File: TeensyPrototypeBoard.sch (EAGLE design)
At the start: 50 parts, among them Q1 16mhz, SW1 SPST_TACT-KMR2, SW2 SPST_TACT-KMR2, U3 BLE112-A, U4 MPU-6050-1, X1 32.768khz

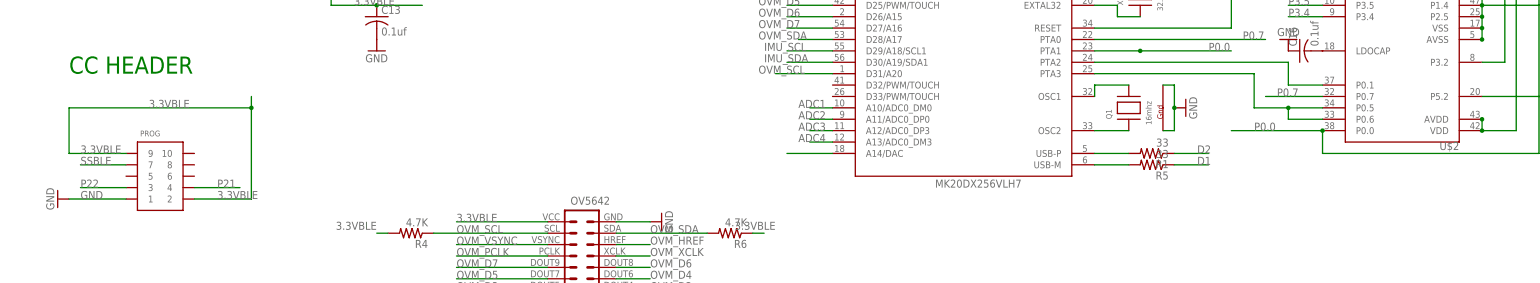
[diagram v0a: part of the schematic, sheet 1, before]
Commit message: connect the oscillator and add generate BOM.txt
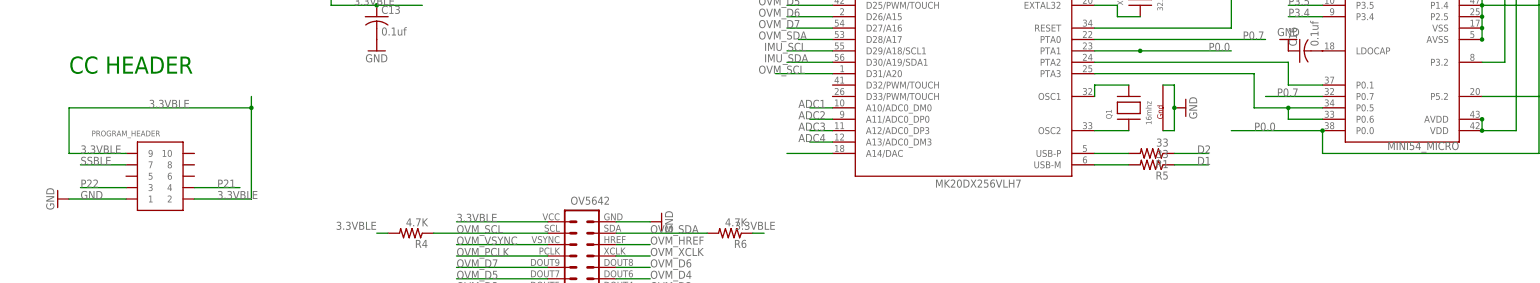
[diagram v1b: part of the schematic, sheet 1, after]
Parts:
- renumbered PROG to PROGRAM_HEADER, U$2 to MINI54_MICRO, U$3 to MICRO_SD_CARD_SINK, U4 to IMU
